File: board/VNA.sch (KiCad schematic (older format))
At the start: 83 parts, among them J1 Conn_02x07_Odd_Even, J10 Conn_01x01, J11 Conn_01x01, J12 Conn_01x01, J13 Barrel_Jack, J14 Conn_01x02, J15 Conn_02x05_Odd_Even, J17 Conn_01x04, J18 Conn_01x01, J19 Conn_01x01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

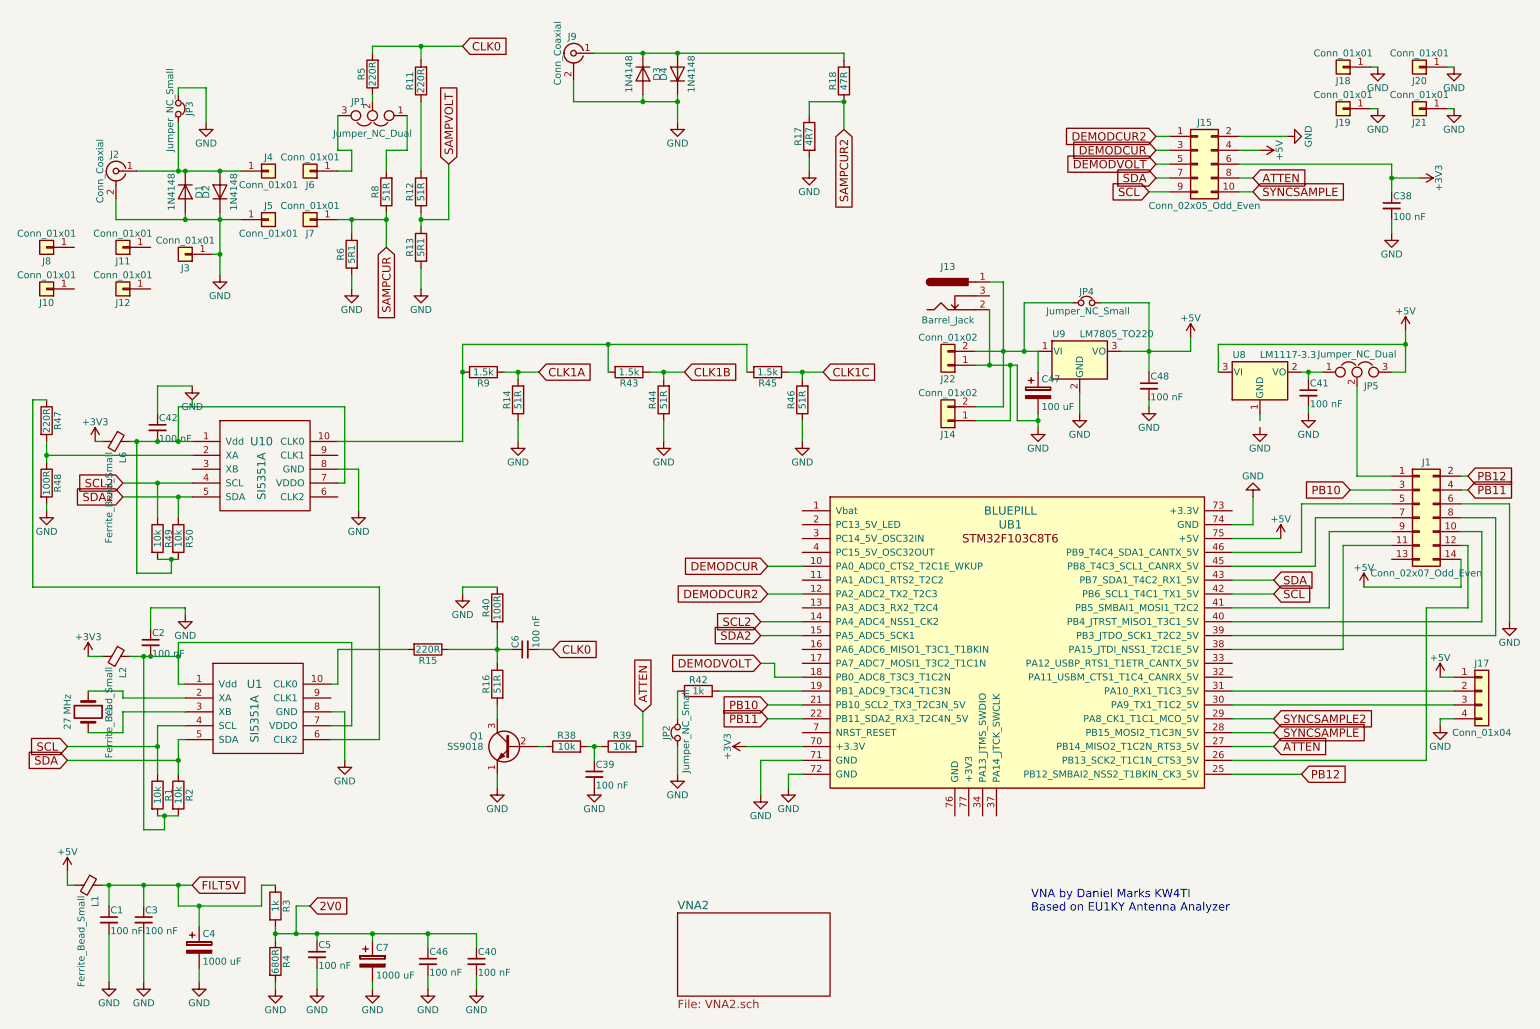
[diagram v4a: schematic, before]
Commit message: Added SD card slot, reorganized pins
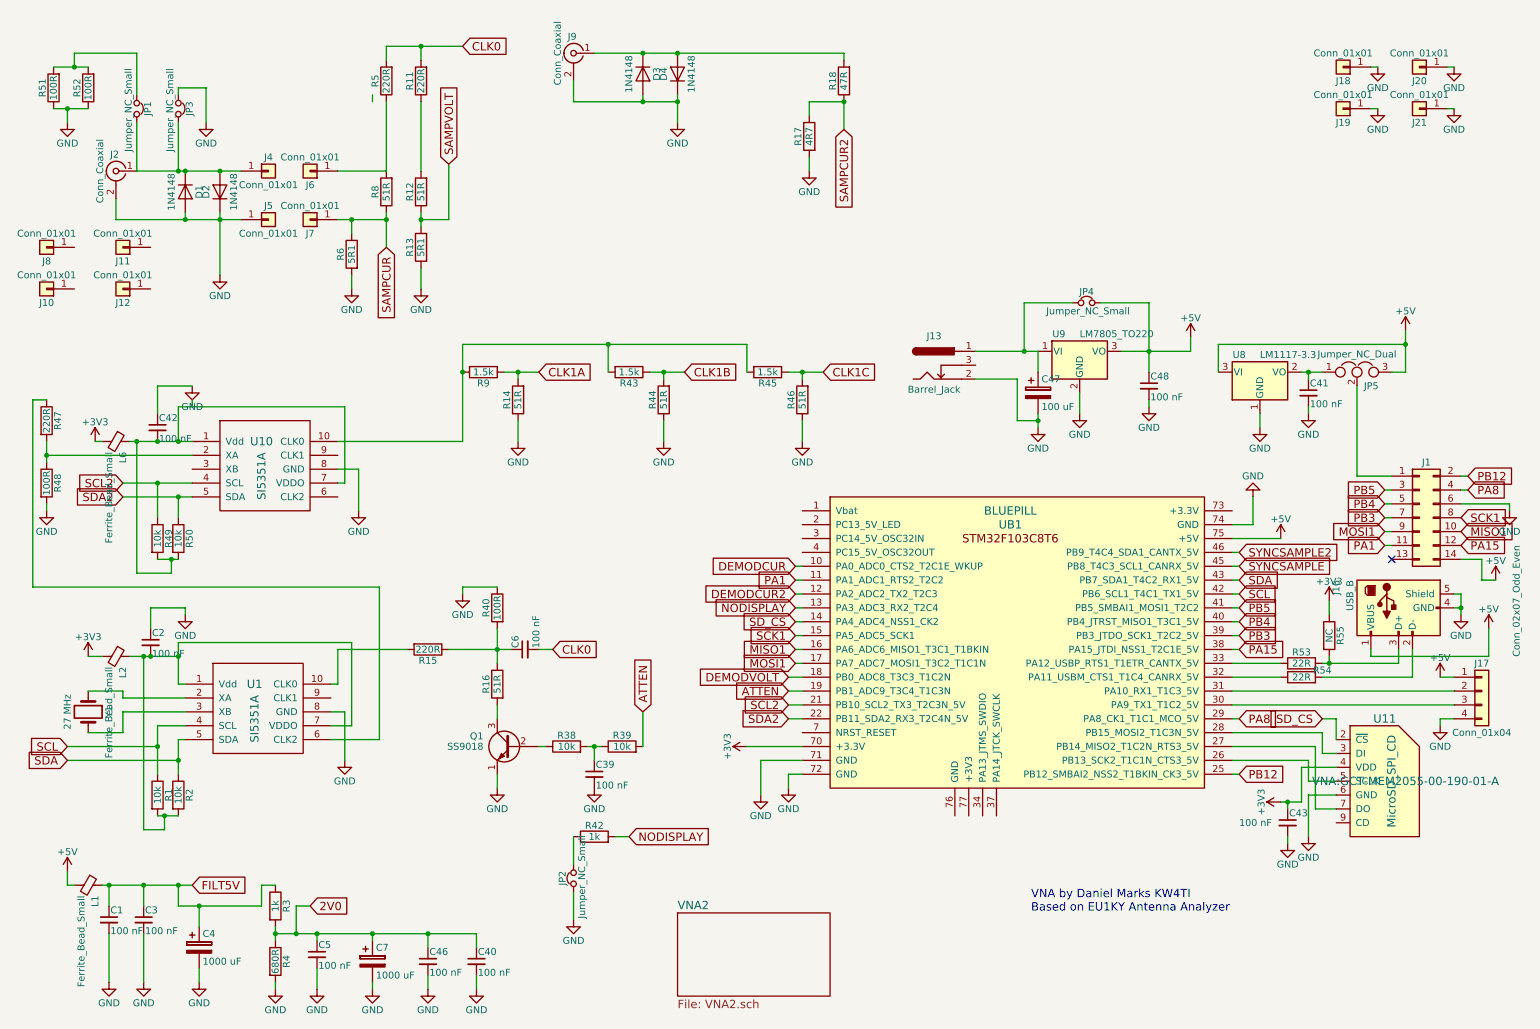
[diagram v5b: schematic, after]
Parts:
- removed C38: 100 nF, Capacitors_THT:C_Disc_D5.0mm_W2.5mm_P2.50mm, symbol C_Small
- removed J14: Conn_01x02, Connectors_Molex:Molex_KK-6410-02_02x2.54mm_Straight, symbol Conn_01x02
- removed J15: Conn_02x05_Odd_Even, Pin_Headers:Pin_Header_Straight_2x05_Pitch2.54mm, symbol Conn_02x05_Odd_Even
- removed J22: Conn_01x02, Connectors_Terminal_Blocks:TerminalBlock_bornier-2_P5.08mm, symbol Conn_01x02
- removed J3: Conn_01x01, Connectors:1pin, symbol Conn_01x01
- removed JP1: Jumper_NC_Dual, Pin_Headers:Pin_Header_Straight_1x03_Pitch2.54mm, symbol Jumper_NC_Dual
- added C43: 100 nF, Capacitors_THT:C_Disc_D5.0mm_W2.5mm_P2.50mm, symbol C_Small
- added J16: USB_B, Connectors:USB_B, symbol USB_B
- added JP1: Jumper_NC_Small, Pin_Headers:Pin_Header_Straight_1x02_Pitch2.54mm, symbol Jumper_NC_Small
- added R51, R52: 100R, Resistors_THT:R_Axial_DIN0207_L6.3mm_D2.5mm_P7.62mm_Horizontal, symbol R
- added R53, R54: 22R, Resistors_THT:R_Axial_DIN0207_L6.3mm_D2.5mm_P7.62mm_Horizontal, symbol R
- added R55: NC, Resistors_THT:R_Axial_DIN0207_L6.3mm_D2.5mm_P7.62mm_Horizontal, symbol R
- added U11: MicroSD_SPI_CD, VNA:GCT-MEM2055-00-190-01-A, symbol MicroSD_SPI_CD
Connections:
- net +3V3: now also C43.1, R55.1, U11.4 (VDD)
- net +5V: now also J16.1 (VBUS)
- net ATTEN: now also UB1.19 (PB1_ADC9_T3C4_T1C3N); no longer UB1.27 (PB14_MISO2_T1C2N_RTS3_5V)
- net GND: now also U8.1 (GND), C43.2, J16.4 (GND), J16.5 (Shield), R51.1, R52.1, U11.6 (GND)
- net SCL2: now also UB1.21 (PB10_SCL2_TX3_T2C3N_5V); no longer UB1.14 (PA4_ADC4_NSS1_CK2)
- net SDA2: now also UB1.22 (PB11_SDA2_RX3_T2C4N_5V); no longer UB1.15 (PA5_ADC5_SCK1)
- net SYNCSAMPLE: now also UB1.45 (PB8_T4C3_SCL1_CANRX_5V); no longer UB1.28 (PB15_MOSI2_T1C3N_5V)
- net SYNCSAMPLE2: now also UB1.46 (PB9_T4C4_SDA1_CANTX_5V); no longer UB1.29 (PA8_CK1_T1C1_MCO_5V)
- net PA1: now reaches UB1.11 (PA1_ADC1_RTS2_T2C2)
- net PA1: now also J1.11 (Pin_11)
- net NODISPLAY: now reaches UB1.13 (PA3_ADC3_RX2_T2C4)
- net NODISPLAY: now also R42.2
- net MISO1: now reaches UB1.16 (PA6_ADC6_MISO1_T3C1_T1BKIN)
- net MISO1: now also J1.10 (Pin_10)
- net MOSI1: now reaches UB1.17 (PA7_ADC7_MOSI1_T3C2_T1C1N)
- net MOSI1: now also J1.9 (Pin_9)
- net at UB1.26 (PB13_SCK2_T1C1N_CTS3_5V): now also U11.5 (SCLK); no longer J1.12 (Pin_12)
- net at UB1.32 (PA11_USBM_CTS1_T1C4_CANRX_5V): now also R54.1
- net at UB1.33 (PA12_USBP_RTS1_T1ETR_CANTX_5V): now also R53.1
- net PA15: now reaches UB1.38 (PA15_JTDI_NSS1_T2C1E_5V)
- net PA15: now also J1.12 (Pin_12); no longer J1.11 (Pin_11)
- net PB3: now reaches UB1.39 (PB3_JTDO_SCK1_T2C2_5V)
- net PB3: now also J1.7 (Pin_7); no longer J1.8 (Pin_8)
- net PB4: now reaches UB1.40 (PB4_JTRST_MISO1_T3C1_5V)
- net PB4: now also J1.5 (Pin_5); no longer J1.10 (Pin_10)
- net PB5: now reaches UB1.41 (PB5_SMBAI1_MOSI1_T2C2)
- net PB5: now also J1.3 (Pin_3); no longer J1.9 (Pin_9)
- net at D1.1 (K), D2.2 (A), J2.1 (In)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: now also JP1.2
- net at J6.1 (Pin_1): now also R5.1, R8.2
- removed net PB10: J1.3 (Pin_3), UB1.21 (PB10_SCL2_TX3_T2C3N_5V)
- net PB11 renamed PA8
- net PA8: now also UB1.29 (PA8_CK1_T1C1_MCO_5V); no longer UB1.22 (PB11_SDA2_RX3_T2C4N_5V)
- new net: U11.7 (DO), UB1.27 (PB14_MISO2_T1C2N_RTS3_5V)
- new net: U11.3 (DI), UB1.28 (PB15_MOSI2_T1C3N_5V)
- new net: JP1.1, R51.2, R52.2
- new net: J16.3 (D+), R53.2, R55.2
- new net: J16.2 (D-), R54.2
- new net SCK1: J1.8 (Pin_8), UB1.15 (PA5_ADC5_SCK1)
- new net SD_CS: U11.2 (~CS), UB1.14 (PA4_ADC4_NSS1_CK2)
- no-connect marks 0 -> 1
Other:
- moved on the sheet: J13, JP2, R42, R5

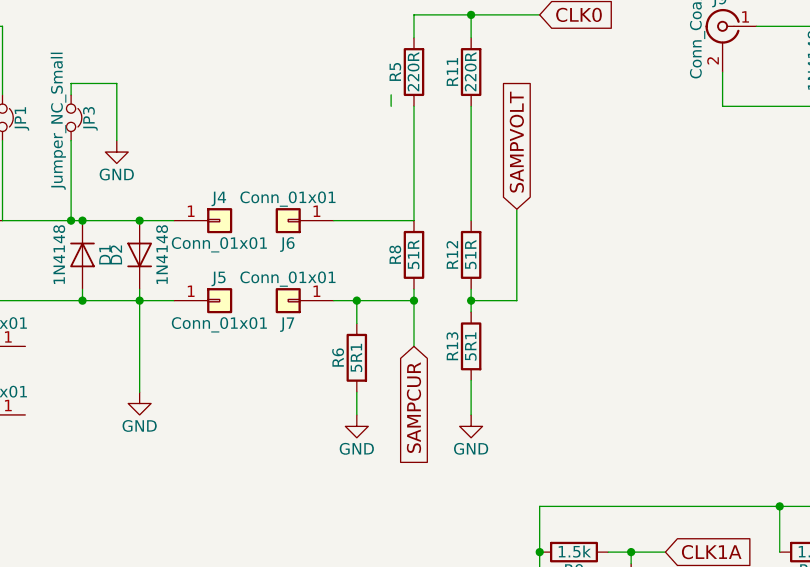
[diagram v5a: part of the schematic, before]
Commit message: Adds SD card support, which is mandatory.  Also changed firmware for new pinouts.
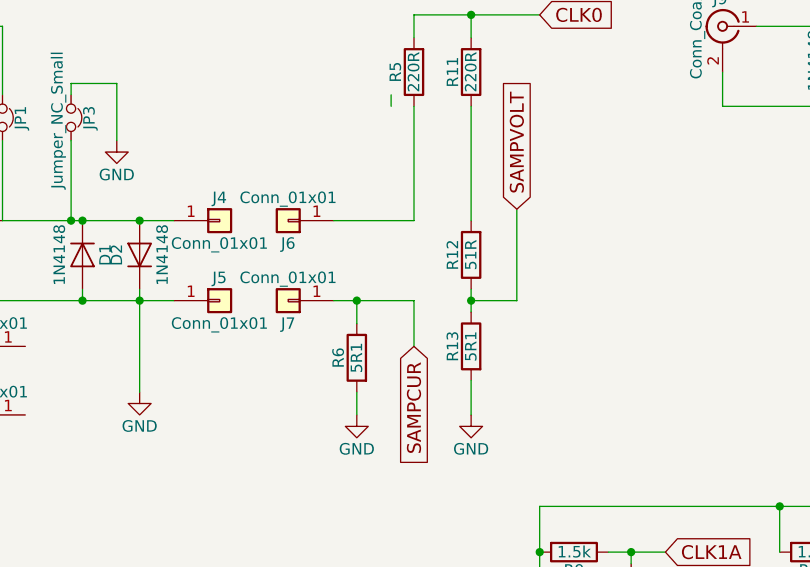
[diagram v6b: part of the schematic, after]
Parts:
- removed R8: 51R, Resistors_THT:R_Axial_DIN0207_L6.3mm_D2.5mm_P7.62mm_Horizontal, symbol R
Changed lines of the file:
@@
 	1    0    0    -1
-$EndComp
-$Comp
-L R R8
-U 1 1 5BB20F66
-P 3100 1700
-F 0 "R8" V 3180 1700 50  0000 C CNN
-F 1 "51R" V 3100 1700 50  0000 C CNN
-F 2 "Resistors_THT:R_Axial_DIN0207_L6.3mm_D2.5mm_P7.62mm_Horizontal" V 3030 1700 50  0001 C CNN
-F 3 "" H 3100 1700 50  0001 C CNN
-	1    3100 1700
-	-1   0    0    1
 $EndComp
 Text GLabel 3100 2100 3    60   Input ~ 0
@@
 Wire Wire Line
 	2750 1550 3100 1550
-Connection ~ 3100 1900
 Connection ~ 2850 1900
 Wire Wire Line
-	3100 1850 3100 2100
+	3100 1900 3100 2100
 Wire Wire Line
 	2750 1900 3100 1900

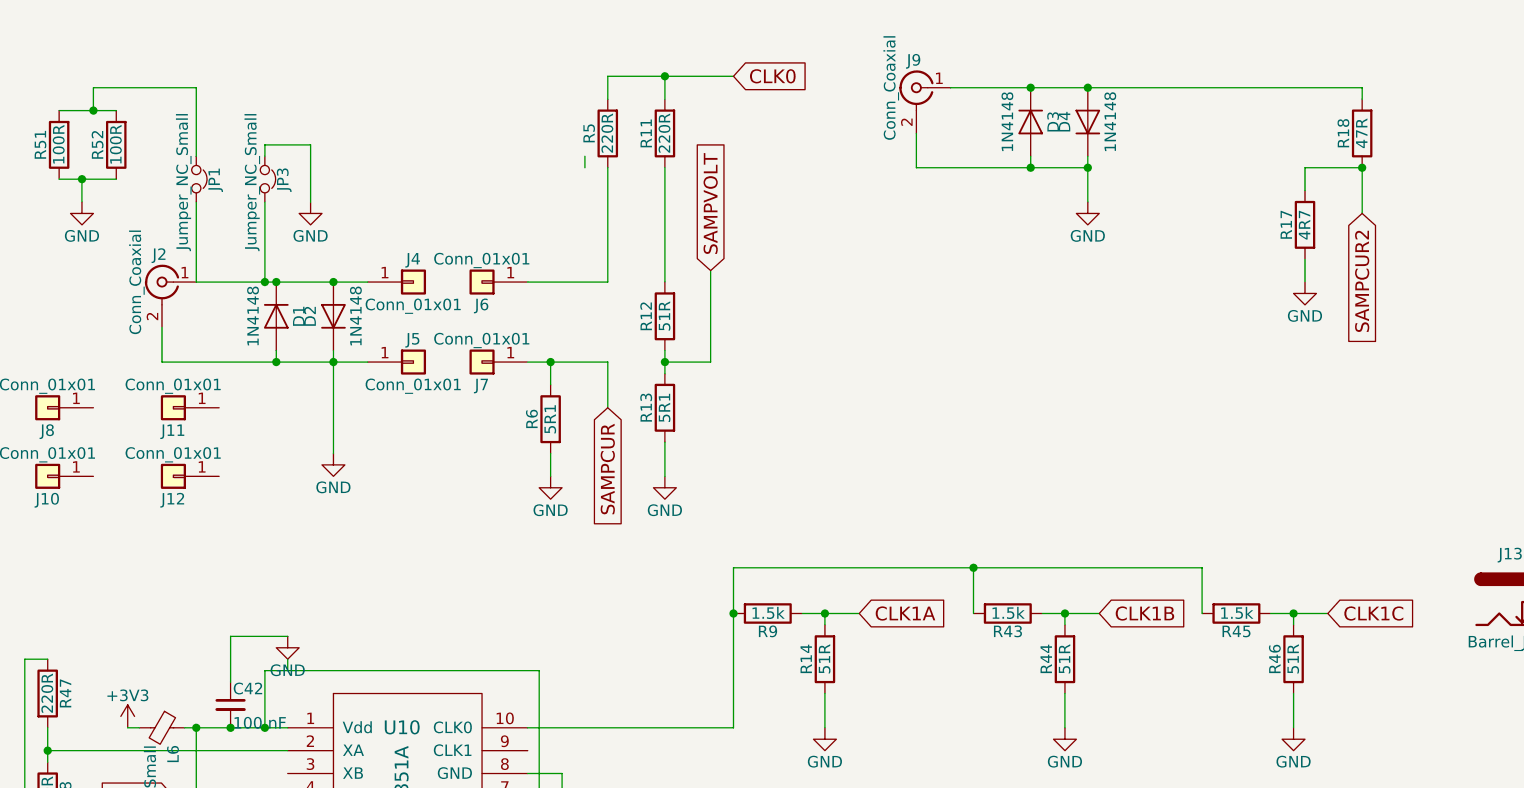
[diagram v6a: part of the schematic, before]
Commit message: Changed to resistive bridge
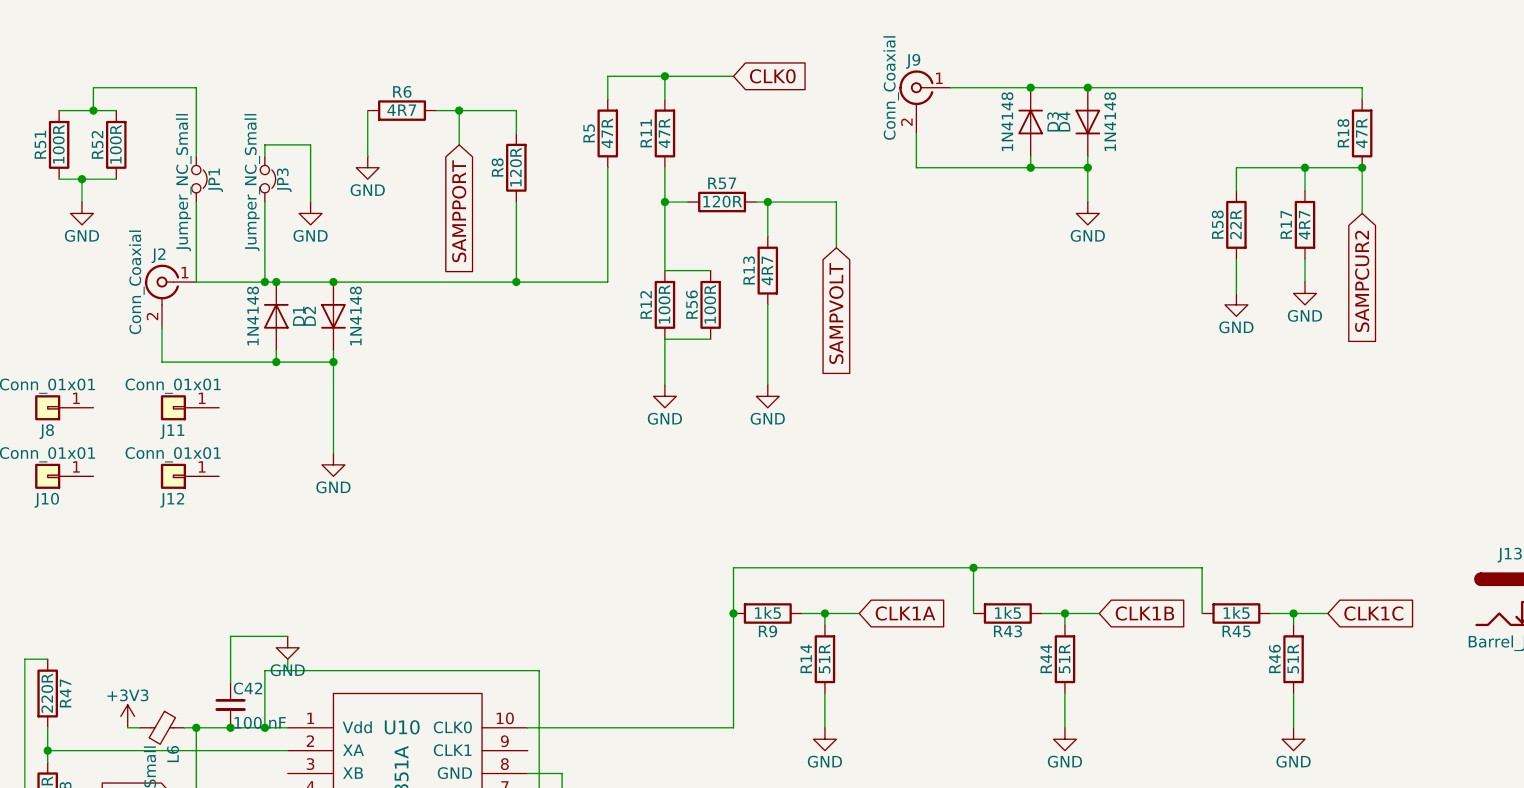
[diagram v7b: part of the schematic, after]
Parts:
- removed J4, J5, J6, J7: Conn_01x01, Connectors:1pin, symbol Conn_01x01
- added R56: 100R, Resistors_THT:R_Axial_DIN0207_L6.3mm_D2.5mm_P7.62mm_Horizontal, symbol R
- added R57, R8: 120R, Resistors_THT:R_Axial_DIN0207_L6.3mm_D2.5mm_P7.62mm_Horizontal, symbol R
- added R58: 22R, Resistors_THT:R_Axial_DIN0207_L6.3mm_D2.5mm_P7.62mm_Horizontal, symbol R
- R11, R5: value 220R -> 47R
- R12: value 51R -> 100R
- R13, R6: value 5R1 -> 4R7
- R43, R45, R9: value 1.5k -> 1k5
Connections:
- net GND: now also R12.1, R56.1, R58.2
- net SAMPCUR2: now also R58.1
- net SAMPVOLT: now also R57.2; no longer R12.1
- net at D1.1 (K), D2.2 (A), J2.1 (In)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: now also R5.1, R8.1
- net at R11.1, R12.2: now also R56.2, R57.1
- net SAMPCUR renamed SAMPPORT
- net SAMPPORT: now also R8.2
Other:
- moved on the sheet: R12, R13, R6
